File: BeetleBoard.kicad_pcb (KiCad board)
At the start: 2 copper layers, 93.8 x 69.5 mm, 61 parts, among them J1 Battery Connector, J10 VBAT_ESC_C, J11 VBAT_ESC_E, J12 VBAT_ESC_F, J13 VBAT_ESC_G, J14 VBAT_ESC_D, J15 VBAT_ESC_H, J16 ESC G, J17 ESC H, J18 ELRS Reciever, J2 ESC A, J3 ESC B, J4 ESC C, J5 ESC D, J6 ESC E, J7 ESC F, J8 VBAT_ESC_A, J9 VBAT_ESC_B, SW1 FingerTech Switch, U1 XIAO-ESP32-C6-SMD, U2 TPS563200, U3 LSM6DSV320XTR

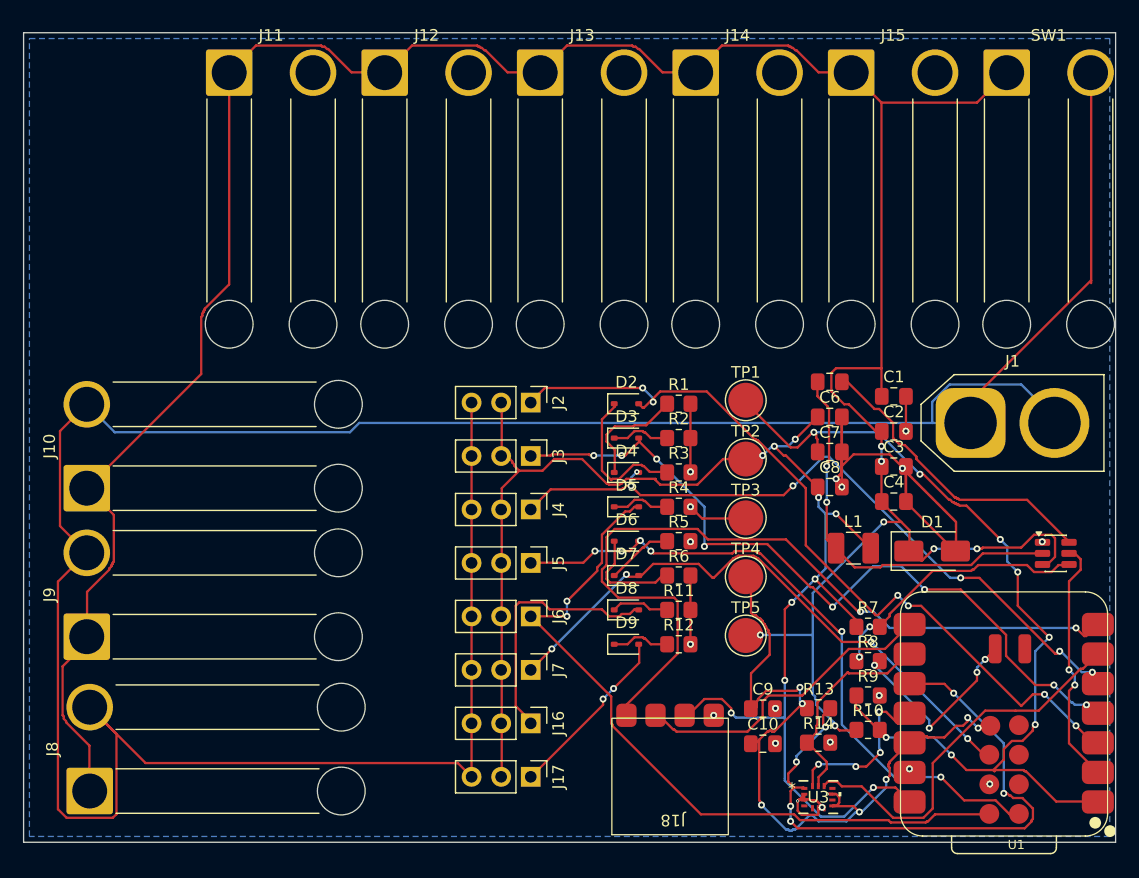
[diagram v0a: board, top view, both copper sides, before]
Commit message: Reorganise PCB and make it neat
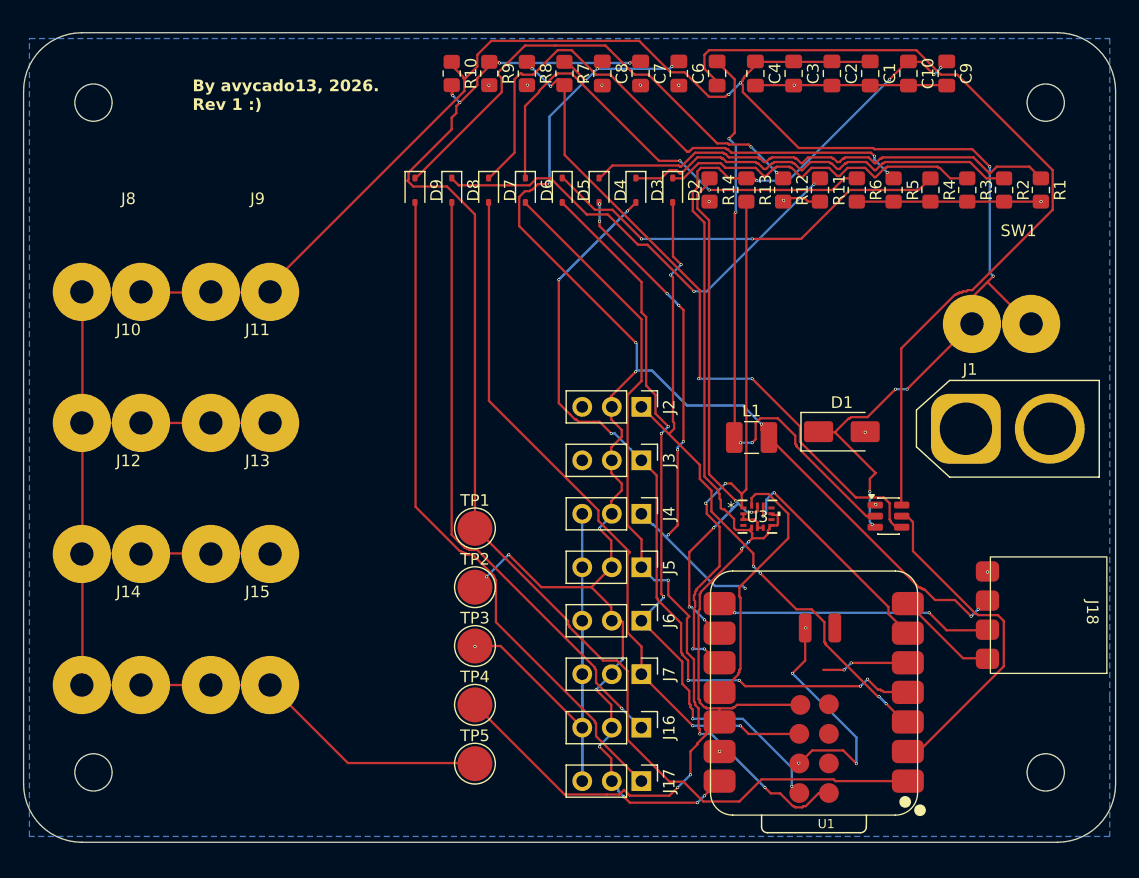
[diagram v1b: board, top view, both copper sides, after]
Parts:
- added G***: LOGO, footprints:dinohat, B.Cu at (176.3, 84.0)
- added REF**: MountingHole_3.2mm_M3, MountingHole:MountingHole_3.2mm_M3, F.Cu at (220.5, 78.5)
- added REF**: MountingHole_3.2mm_M3, MountingHole:MountingHole_3.2mm_M3, F.Cu at (138.8, 136.0)
- added REF**: MountingHole_3.2mm_M3, MountingHole:MountingHole_3.2mm_M3, F.Cu at (220.5, 136.0)
- added REF**: MountingHole_3.2mm_M3, MountingHole:MountingHole_3.2mm_M3, F.Cu at (138.8, 78.5)
- J10, J11, J12, J13, J14, J15, J8, J9, SW1: footprint Connector_Wire:SolderWire-2.5sqmm_1x02_P7.2mm_D2.4mm_OD3.6mm_Relief -> footprints:Power_SolderPad_2Pin_P5.08mm_D2.0mm
- moved J15 68.0 mm to (152.8, 121.0)
- moved R10 66.7 mm to (169.5, 76.0), turned to -90 degrees
- moved J14 66.4 mm to (141.8, 121.0)
- moved R9 62.5 mm to (172.7, 76.0), turned to -90 degrees
- moved C10 58.9 mm to (208.7, 76.0), turned to -90 degrees
- moved R8 58.3 mm to (176.0, 76.0), turned to -90 degrees
- moved C9 56.8 mm to (212.0, 76.0), turned to -90 degrees
- moved R7 54.2 mm to (179.2, 76.0), turned to -90 degrees
- moved J8 50.5 mm to (141.8, 87.2), turned to 0 degrees
- moved R14 48.4 mm to (191.6, 86.0), turned to -90 degrees
- moved R13 44.9 mm to (194.8, 86.0), turned to -90 degrees
- moved D9 43.0 mm to (166.3, 86.0), turned to -90 degrees
- moved J13 41.6 mm to (152.8, 109.8)
- moved C8 40.5 mm to (182.4, 76.0), turned to -90 degrees
- moved J12 40.4 mm to (141.8, 109.8)
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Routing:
- net GND: track 299.8 -> 109.1 mm, vias 22 -> 19
- net /XIAO_TX: track 68.1 -> 8.83 mm, vias 2 -> 0
- net +3V3: track 64.8 -> 121.7 mm
- net /Power/VBST: track 26.1 -> 72.2 mm
- net /ESC_H: track 15.3 -> 58.3 mm, vias 2 -> 0
- net Net-(D7-A1): track 5.80 -> 48.1 mm, vias 0 -> 2
- net Net-(D9-A1): track 5.04 -> 42.6 mm, vias 0 -> 2
- net /VBAT_SNS: track 79.2 -> 116.2 mm, vias 8 -> 4
- net /Power/VFB: track 23.7 -> 59.2 mm, vias 2 -> 4
- net Net-(D8-A1): track 5.03 -> 40.2 mm, vias 0 -> 2
- net Net-(J1-Pin_1): track 34.5 -> 0.00 mm
- net Net-(D4-A1): track 9.88 -> 41.8 mm
- net Net-(D6-A1): track 9.21 -> 40.5 mm, vias 0 -> 2
- net Net-(D5-A1): track 5.04 -> 36.0 mm, vias 0 -> 2
- net Net-(D3-A1): track 5.04 -> 35.5 mm
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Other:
- outline, holes or cut-outs redrawn
- board text added: "By avycado13, 2026. Rev 1 :)"

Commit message: make pcb nicer and add firmware written by ai
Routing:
- net VBUS: track 257.6 -> 374.1 mm
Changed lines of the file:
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@@
+	)
+	(segment
+		(start 153.91 128.5)
+		(end 148.83 128.5)
+		(width 0.1998)
+		(layer "F.Cu")
+		(net "VBUS")
 	)
 	(segment
@@
 	)
 	(segment
+		(start 153.91 106)
+		(end 148.83 106)
+		(width 0.1998)
+		(layer "F.Cu")
+		(net "VBUS")
+	)
+	(segment
 		(start 194.5 77.6)
 		(end 199.3 82.4)
@@
 	)
 	(segment
+		(start 153.91 128.5)
+		(end 153.91 94.75)
+		(width 0.1998)
+		(layer "F.Cu")
+		(net "VBUS")
+	)
+	(segment
 		(start 180.2 73.2)
 		(end 185.6 73.2)
@@
 	)
 	(segment
+		(start 142.83 94.75)
+		(end 142.83 128.5)
+		(width 0.1998)
+		(layer "F.Cu")
+		(net "VBUS")
+	)
+	(segment
 		(start 148.8 94.8)
 		(end 142.8 94.8)
@@
 	)
 	(segment
+		(start 153.91 117.25)
+		(end 148.83 117.25)
+		(width 0.1998)
+		(layer "F.Cu")
+		(net "VBUS")
+	)
+	(segment
 		(start 202.1 75)
 		(end 202.144926 74.9625)
@@
 		(width 0.1998)
 		(layer "F.Cu")
+		(net "VBUS")
+	)
+	(segment
+		(start 148.83 94.75)
+		(end 148.83 128.5)
+		(width 0.1998)
+		(layer "F.Cu")

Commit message: Thicken power traces and some cleanup
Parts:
- moved C9 51.8 mm to (163.5, 94.2), turned to 0 degrees
- moved C8 51.4 mm to (163.5, 123.8), turned to 0 degrees
- moved C10 50.1 mm to (163.5, 97.5), turned to 0 degrees
- moved C7 49.7 mm to (163.5, 120.5), turned to 0 degrees
- moved C1 48.7 mm to (163.5, 100.8), turned to 0 degrees
- moved C6 48.4 mm to (163.5, 117.2), turned to 0 degrees
- moved C2 47.7 mm to (163.5, 104.0), turned to 0 degrees
- moved C5 47.6 mm to (163.5, 113.9), turned to 0 degrees
- moved C3 47.2 mm to (163.5, 107.3), turned to 0 degrees
- moved C4 47.2 mm to (163.5, 110.6), turned to 0 degrees
- moved R9 20.0 mm to (176.0, 95.8)
- moved R10 19.8 mm to (169.5, 95.8)
- moved U2 2.86 mm to (204.1, 114.0)
- moved SW1 0.25 mm to (217.9, 90.0)
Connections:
- SW1 pad 1: VBUS -> Net-(J1-Pin_1)
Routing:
- net VBUS: track 374.1 -> 234.1 mm, vias 8 -> 7
- net GND: track 109.1 -> 237.5 mm, vias 19 -> 61
- net /Power/VBST: track 72.2 -> 96.6 mm, vias 0 -> 4
- net /VBAT_SNS: track 116.2 -> 92.2 mm, vias 4 -> 2
- net /ESC_H: track 58.3 -> 72.5 mm, vias 0 -> 3
- net /ESC_C: track 51.5 -> 64.6 mm, vias 10 -> 6
- net /ESC_G: track 52.4 -> 65.0 mm, vias 1 -> 4
- net +3V3: track 121.7 -> 132.3 mm
- net Net-(J1-Pin_1): track 0.00 -> 9.11 mm
- net +5V: track 148.4 -> 155.5 mm, vias 18 -> 9
- net /ESC_A: track 58.5 -> 64.1 mm
- net /SPI_MISO: track 47.4 -> 52.6 mm, vias 4 -> 7
- net Net-(D9-A1): track 42.6 -> 37.9 mm
- net Net-(D8-A1): track 40.2 -> 44.7 mm, vias 2 -> 4
- net /ESC_B: track 69.5 -> 65.8 mm, vias 7 -> 6
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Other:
- board text added: "By avycado13, 2026. Rev 1.1 :)"
